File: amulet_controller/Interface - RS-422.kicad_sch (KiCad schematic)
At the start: 2 parts, among them U11 SN65HVD35DR

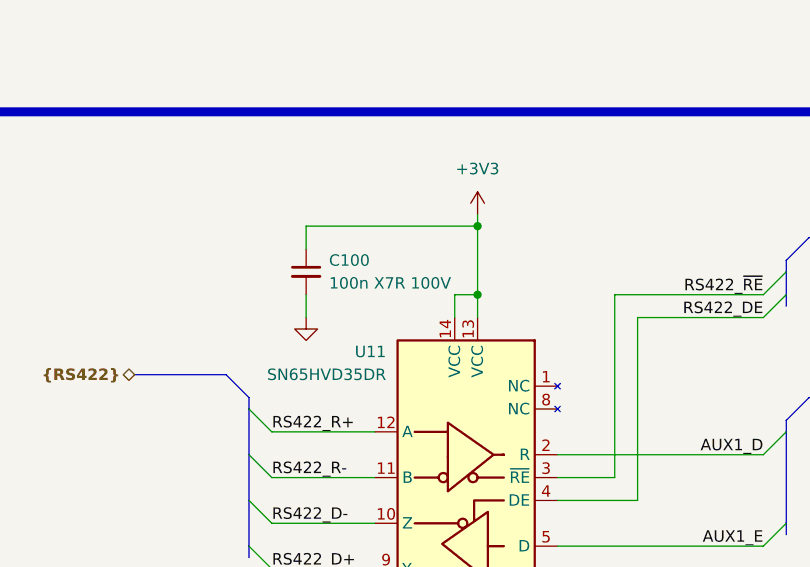
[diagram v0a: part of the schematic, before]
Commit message: filled in fields for bom, replaced inexisting components. Need to replace LEDs
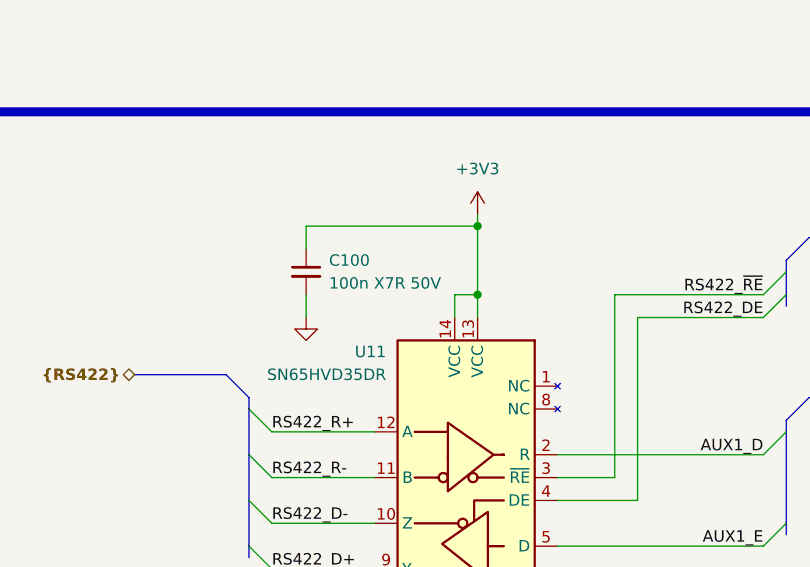
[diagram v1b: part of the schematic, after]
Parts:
- C100: value 100n X7R 100V -> 100n X7R 50V; Manufacturer (none) -> Murata Electronics; Manufacturer Part Number (none) -> GCM155R71H104KE02J; Supplier 1 (none) -> Digikey; Supplier Part Number 1 (none) -> 490-14514-1-ND
- U11: Manufacturer (none) -> Texas Instruments; Manufacturer Part Number (none) -> SN65HVD35DR; Supplier 1 (none) -> Digikey; Supplier Part Number 1 (none) -> 296-18706-1-ND
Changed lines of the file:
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@@
     (pin "1")
     (instances
-      (project "bldc_controller"
+      (project "amulet_controller"
         (path "/0650c7a8-acba-429c-9f8e-eec0baf0bc1c/fede4c36-00cc-4d3d-b71c-5243ba232202/a62105fd-dfaf-4ee0-a401-8aa0e7120758"
           (reference "#PWR052") (unit 1)
@@
       (effects (font (size 1.27 1.27)) (justify left))
     )
-    (property "Value" "100n X7R 100V" (at 130.81 60.9663 0)
+    (property "Value" "100n X7R 50V" (at 130.81 60.9663 0)
       (effects (font (size 1.27 1.27)) (justify left))
     )
@@
       (effects (font (size 1.27 1.27)) hide)
     )
-    (property "Datasheet" "~" (at 128.27 59.69 0)
+    (property "Datasheet" "https://search.murata.co.jp/Ceramy/image/img/A01X/G101/ENG/GCM155R71H104KE02-01.pdf" (at 128.27 59.69 0)
+      (effects (font (size 1.27 1.27)) hide)
+    )
+    (property "Description" "0.1 µF ±10% 50V Ceramic Capacitor X7R 0402 (1005 Metric)" (at 128.27 59.69 0)
+      (effects (font (size 1.27 1.27)) hide)
+    )
+    (property "Manufacturer" "Murata Electronics" (at 128.27 59.69 0)
+      (effects (font (size 1.27 1.27)) hide)
+    )
+    (property "Manufacturer Part Number" "GCM155R71H104KE02J" (at 128.27 59.69 0)
+      (effects (font (size 1.27 1.27)) hide)
+    )
+    (property "Supplier 1" "Digikey" (at 128.27 59.69 0)
+      (effects (font (size 1.27 1.27)) hide)
+    )
+    (property "Supplier Part Number 1" "490-14514-1-ND" (at 128.27 59.69 0)
       (effects (font (size 1.27 1.27)) hide)
     )
@@
     (pin "2")
     (instances
-      (project "bldc_controller"
+      (project "amulet_controller"
         (path "/0650c7a8-acba-429c-9f8e-eec0baf0bc1c/fede4c36-00cc-4d3d-b71c-5243ba232202/a62105fd-dfaf-4ee0-a401-8aa0e7120758"
           (reference "C100") (unit 1)
@@
     (pin "1")
     (instances
-      (project "bldc_controller"
+      (project "amulet_controller"
         (path "/0650c7a8-acba-429c-9f8e-eec0baf0bc1c/fede4c36-00cc-4d3d-b71c-5243ba232202/a62105fd-dfaf-4ee0-a401-8aa0e7120758"
           (reference "#PWR050") (unit 1)
@@
     (pin "1")
     (instances
-      (project "bldc_controller"
+      (project "amulet_controller"
         (path "/0650c7a8-acba-429c-9f8e-eec0baf0bc1c/fede4c36-00cc-4d3d-b71c-5243ba232202/a62105fd-dfaf-4ee0-a401-8aa0e7120758"
           (reference "#PWR051") (unit 1)
@@
       (effects (font (size 1.27 1.27)) hide)
     )
+    (property "Description" "SN65HVD3x 3.3-V Full-Duplex RS-485 Drivers and Receivers" (at 146.05 85.09 0)
+      (effects (font (size 1.27 1.27)) hide)
+    )
+    (property "Manufacturer" "Texas Instruments" (at 146.05 85.09 0)
+      (effects (font (size 1.27 1.27)) hide)
+    )
+    (property "Manufacturer Part Number" "SN65HVD35DR" (at 146.05 85.09 0)
+      (effects (font (size 1.27 1.27)) hide)
+    )
+    (property "Supplier 1" "Digikey" (at 146.05 85.09 0)
+      (effects (font (size 1.27 1.27)) hide)
+    )
+    (property "Supplier Part Number 1" "296-18706-1-ND" (at 146.05 85.09 0)
+      (effects (font (size 1.27 1.27)) hide)
+    )
     (pin "1")
     (pin "10")
@@
     (pin "9")
     (instances
-      (project "bldc_controller"
+      (project "amulet_controller"
         (path "/0650c7a8-acba-429c-9f8e-eec0baf0bc1c/fede4c36-00cc-4d3d-b71c-5243ba232202/a62105fd-dfaf-4ee0-a401-8aa0e7120758"
           (reference "U11") (unit 1)

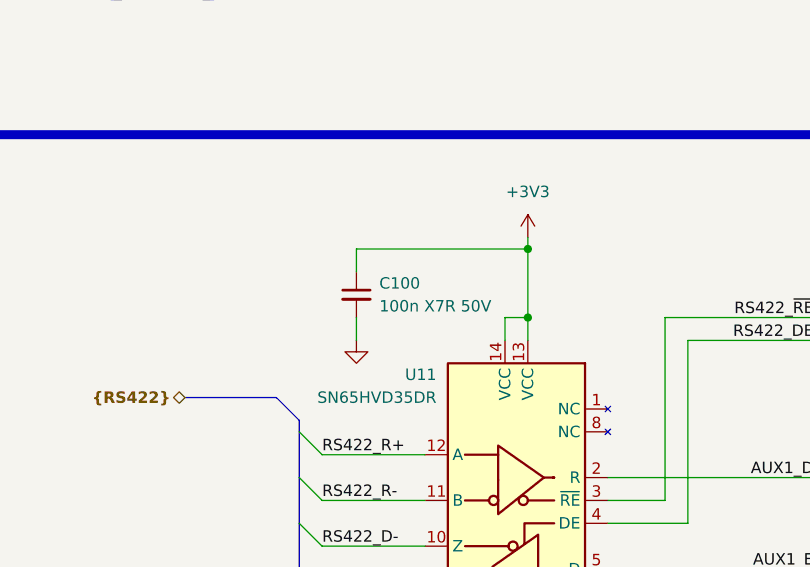
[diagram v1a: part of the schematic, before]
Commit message: finalized pcb. TODO: add clean BOM and KiBot integration
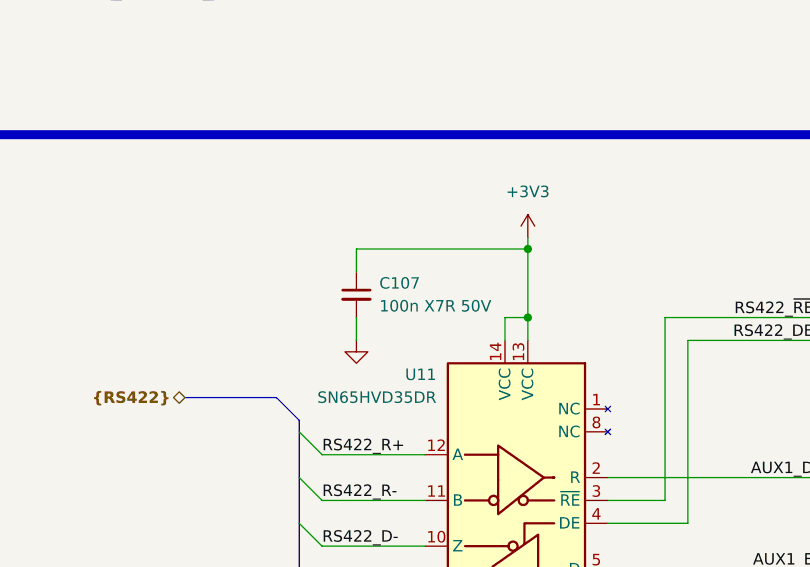
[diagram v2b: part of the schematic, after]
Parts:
- renumbered C100 to C107
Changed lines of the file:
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@@
   (symbol (lib_id "power:+3V3") (at 147.32 53.34 0) (unit 1)
     (in_bom yes) (on_board yes) (dnp no) (fields_autoplaced)
-    (property "Reference" "#PWR052" (at 147.32 57.15 0)
+    (property "Reference" "#PWR053" (at 147.32 57.15 0)
       (effects (font (size 1.27 1.27)) hide)
     )
@@
       (project "amulet_controller"
         (path "/0650c7a8-acba-429c-9f8e-eec0baf0bc1c/fede4c36-00cc-4d3d-b71c-5243ba232202/a62105fd-dfaf-4ee0-a401-8aa0e7120758"
-          (reference "#PWR052") (unit 1)
+          (reference "#PWR053") (unit 1)
         )
       )
@@
   (symbol (lib_id "Device:C_Small") (at 128.27 59.69 0) (unit 1)
     (in_bom yes) (on_board yes) (dnp no) (fields_autoplaced)
-    (property "Reference" "C100" (at 130.81 58.4263 0)
+    (property "Reference" "C107" (at 130.81 58.4263 0)
       (effects (font (size 1.27 1.27)) (justify left))
     )
@@
       (project "amulet_controller"
         (path "/0650c7a8-acba-429c-9f8e-eec0baf0bc1c/fede4c36-00cc-4d3d-b71c-5243ba232202/a62105fd-dfaf-4ee0-a401-8aa0e7120758"
-          (reference "C100") (unit 1)
+          (reference "C107") (unit 1)
         )
       )
@@
   (symbol (lib_id "power:GND") (at 128.27 64.77 0) (unit 1)
     (in_bom yes) (on_board yes) (dnp no) (fields_autoplaced)
-    (property "Reference" "#PWR050" (at 128.27 71.12 0)
+    (property "Reference" "#PWR051" (at 128.27 71.12 0)
       (effects (font (size 1.27 1.27)) hide)
     )
@@
       (project "amulet_controller"
         (path "/0650c7a8-acba-429c-9f8e-eec0baf0bc1c/fede4c36-00cc-4d3d-b71c-5243ba232202/a62105fd-dfaf-4ee0-a401-8aa0e7120758"
-          (reference "#PWR050") (unit 1)
+          (reference "#PWR051") (unit 1)
         )
       )
@@
   (symbol (lib_id "power:GND") (at 146.05 109.22 0) (unit 1)
     (in_bom yes) (on_board yes) (dnp no) (fields_autoplaced)
-    (property "Reference" "#PWR051" (at 146.05 115.57 0)
+    (property "Reference" "#PWR052" (at 146.05 115.57 0)
       (effects (font (size 1.27 1.27)) hide)
     )
@@
       (project "amulet_controller"
         (path "/0650c7a8-acba-429c-9f8e-eec0baf0bc1c/fede4c36-00cc-4d3d-b71c-5243ba232202/a62105fd-dfaf-4ee0-a401-8aa0e7120758"
-          (reference "#PWR051") (unit 1)
+          (reference "#PWR052") (unit 1)
         )
       )

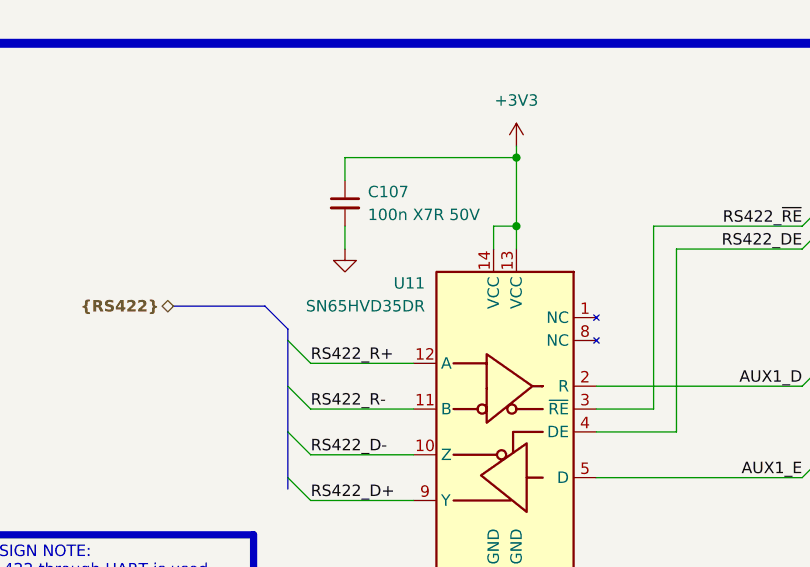
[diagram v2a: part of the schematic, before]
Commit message: corrected pcb according to reviews on reddit
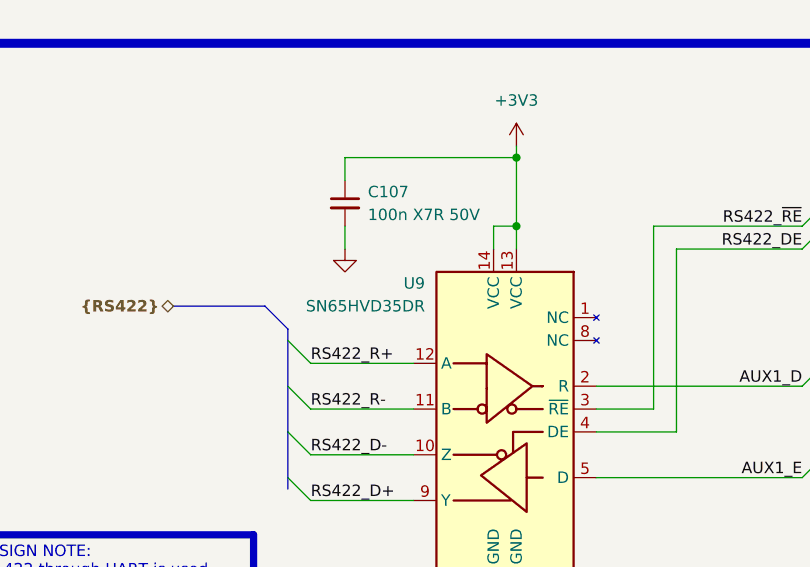
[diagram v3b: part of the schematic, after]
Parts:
- renumbered U11 to U9
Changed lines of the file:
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@@
   (symbol (lib_id "power:+3V3") (at 147.32 53.34 0) (unit 1)
     (in_bom yes) (on_board yes) (dnp no) (fields_autoplaced)
-    (property "Reference" "#PWR053" (at 147.32 57.15 0)
+    (property "Reference" "#PWR054" (at 147.32 57.15 0)
       (effects (font (size 1.27 1.27)) hide)
     )
@@
       (project "amulet_controller"
         (path "/0650c7a8-acba-429c-9f8e-eec0baf0bc1c/fede4c36-00cc-4d3d-b71c-5243ba232202/a62105fd-dfaf-4ee0-a401-8aa0e7120758"
-          (reference "#PWR053") (unit 1)
+          (reference "#PWR054") (unit 1)
         )
       )
@@
   (symbol (lib_id "power:GND") (at 128.27 64.77 0) (unit 1)
     (in_bom yes) (on_board yes) (dnp no) (fields_autoplaced)
-    (property "Reference" "#PWR051" (at 128.27 71.12 0)
+    (property "Reference" "#PWR052" (at 128.27 71.12 0)
       (effects (font (size 1.27 1.27)) hide)
     )
@@
       (project "amulet_controller"
         (path "/0650c7a8-acba-429c-9f8e-eec0baf0bc1c/fede4c36-00cc-4d3d-b71c-5243ba232202/a62105fd-dfaf-4ee0-a401-8aa0e7120758"
-          (reference "#PWR051") (unit 1)
+          (reference "#PWR052") (unit 1)
         )
       )
@@
   (symbol (lib_id "power:GND") (at 146.05 109.22 0) (unit 1)
     (in_bom yes) (on_board yes) (dnp no) (fields_autoplaced)
-    (property "Reference" "#PWR052" (at 146.05 115.57 0)
+    (property "Reference" "#PWR053" (at 146.05 115.57 0)
       (effects (font (size 1.27 1.27)) hide)
     )
@@
       (project "amulet_controller"
         (path "/0650c7a8-acba-429c-9f8e-eec0baf0bc1c/fede4c36-00cc-4d3d-b71c-5243ba232202/a62105fd-dfaf-4ee0-a401-8aa0e7120758"
-          (reference "#PWR052") (unit 1)
+          (reference "#PWR053") (unit 1)
         )
       )
@@
   (symbol (lib_id "0_interface_uart:SN65HVD35DR") (at 146.05 85.09 0) (mirror y) (unit 1)
     (in_bom yes) (on_board yes) (dnp no)
-    (property "Reference" "U11" (at 137.16 68.58 0)
+    (property "Reference" "U9" (at 137.16 68.58 0)
       (effects (font (size 1.27 1.27)) (justify left))
     )
@@
       (project "amulet_controller"
         (path "/0650c7a8-acba-429c-9f8e-eec0baf0bc1c/fede4c36-00cc-4d3d-b71c-5243ba232202/a62105fd-dfaf-4ee0-a401-8aa0e7120758"
-          (reference "U11") (unit 1)
+          (reference "U9") (unit 1)
         )
       )
